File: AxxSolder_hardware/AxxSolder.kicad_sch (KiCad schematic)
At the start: 143 parts, among them IC1 TLV76733DRVR, IC2 OPA2387DSGT, IC3 LMR54406DBVR, IC4 STM32G431CBT6, IC5 TPD4E1U06DBVR, IC6 STUSB4500QTR, IC7 MAX16171ATA_VY+T, IC8 LTC4440AHMS8E, IC9 INA281A5QDBVRQ1, J1 USB4110-GF-A, J2 691243110009, J3 TSW-102-07-T-S, J4 61300611821, J5 TSW-102-07-T-S, J6 TSW-102-07-T-S, Q1 STL9P3LLH6, Q2 STL10N3LLH5, Q3 2N7002NXAKR, U2 PEC11J-9215F-S0015, U3 BSC014N04LS

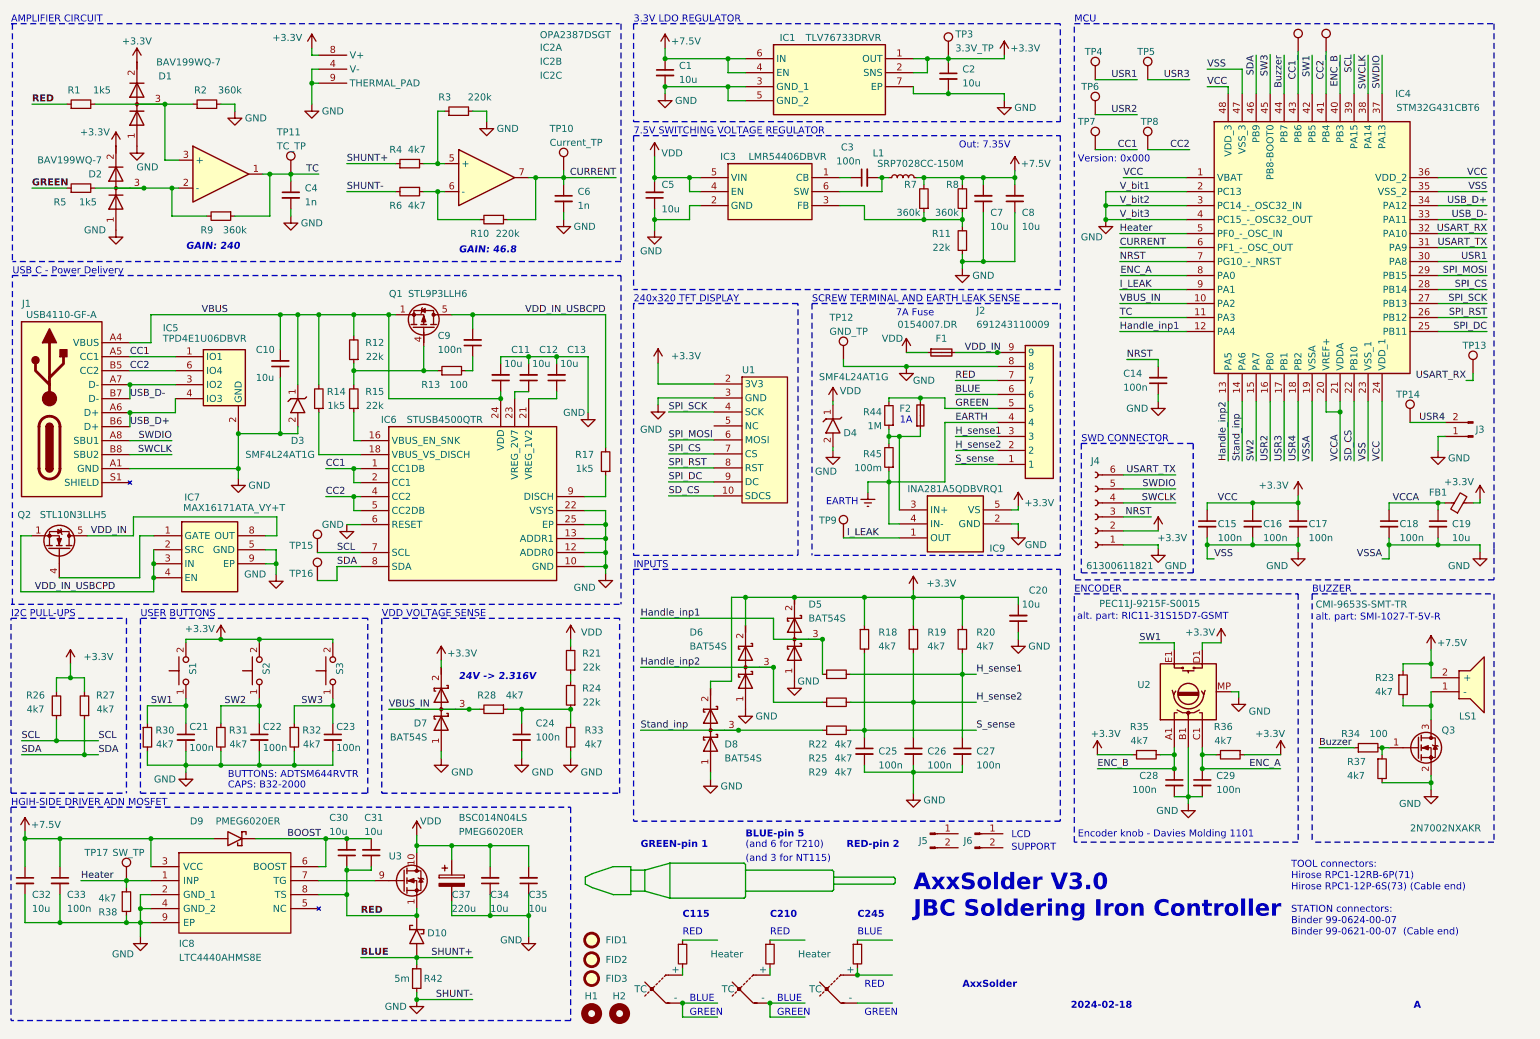
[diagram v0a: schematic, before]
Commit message: Create Lite version of board
Mark all USB-C components as DNP (except I2C pullups)
Swap LCD footprint from Adafruit 4311 to commodity GMT020-02 LCD
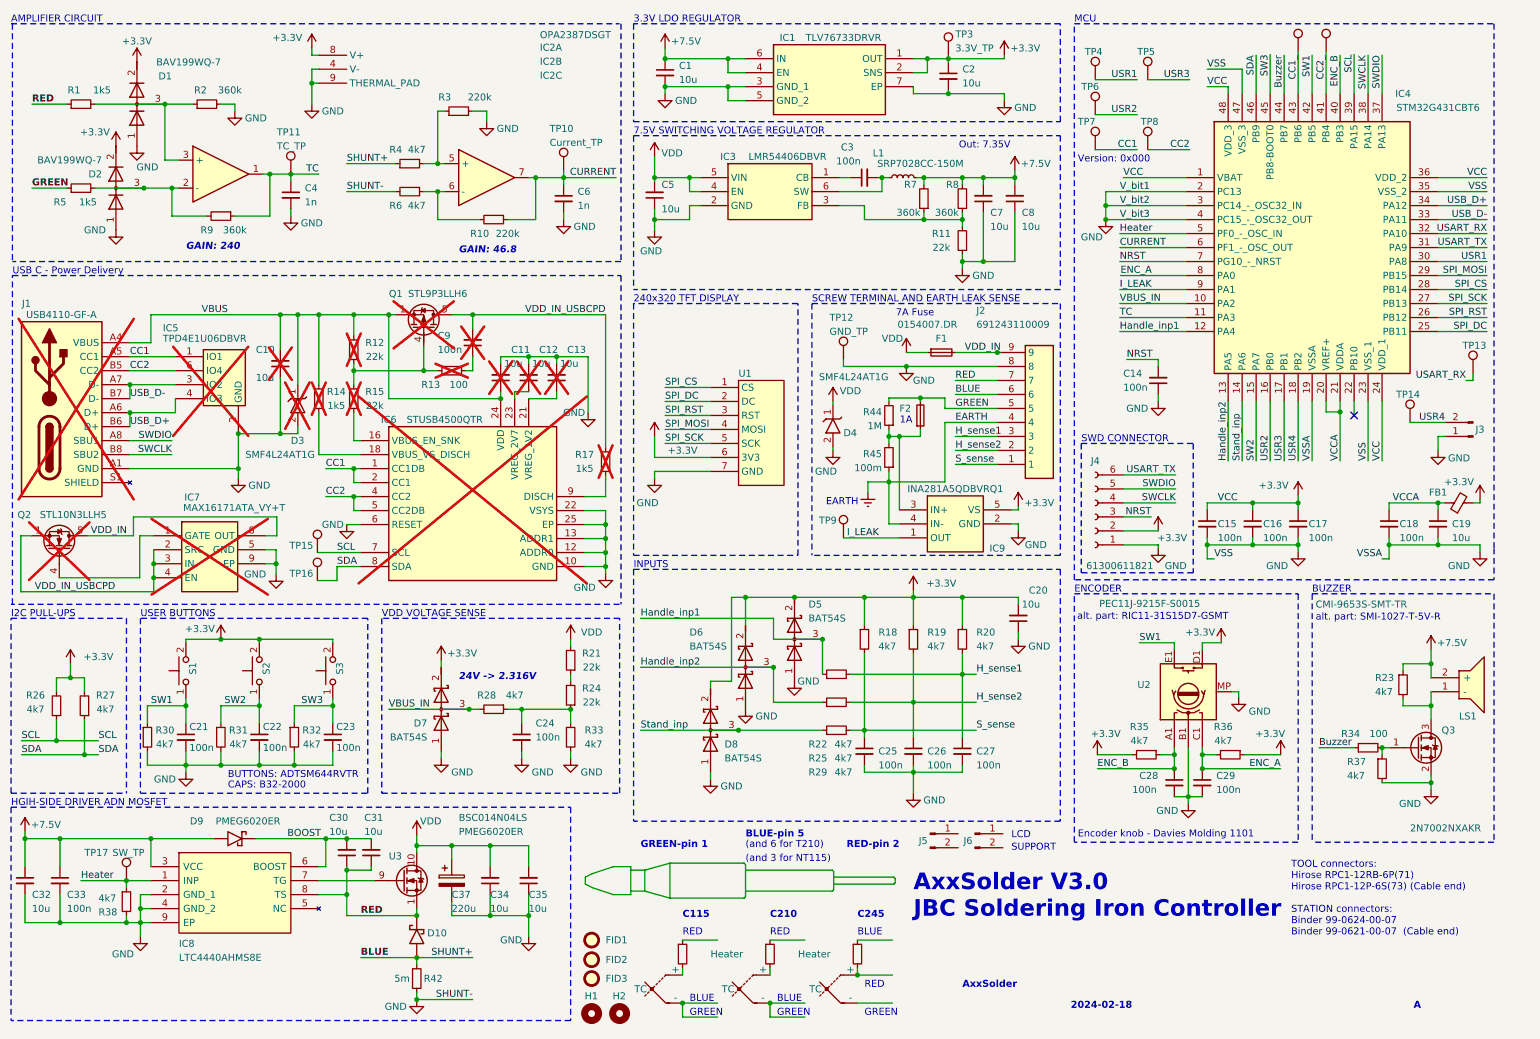
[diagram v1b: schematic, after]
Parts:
- C10, C11, C12, C13, C9, D3, IC6, IC7, Q1, Q2, R12, R13, R14, R15, R17: now not fitted; now left out of the parts list
- C37: footprint CAPAE830X1050N -> footprints:CAPAE830X1050N
- IC3: footprint SOT95P280X145-6N -> footprints:SOT95P280X145-6N
- IC5: footprint SOT95P280X145-6N -> footprints:SOT95P280X145-6N; now not fitted; now left out of the parts list
- J1: footprint USB4110GFA -> footprints:USB4110GFA; now not fitted; now left out of the parts list
- U1: footprint footprints:Adafruit_240x320_TFT -> Connector_PinHeader_2.54mm:PinHeader_1x07_P2.54mm_Vertical; Manufacturer_Name Adafruit -> (none); Manufacturer_Part_Number 4311 -> 2.0TFTSPI; Mouser Part Number 485-4311 -> (none); Mouser Price/Stock https://www.mouser.co.uk/ProductDetail/Adafruit/4311?qs=P1J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 -> (none)
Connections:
- net +3.3V: now also U1.6 (3V3); no longer U1.2 (3V3)
- net GND: now also U1.7 (GND); no longer U1.3 (GND)
- net SPI_CS: now also U1.1 (CS); no longer U1.7 (CS)
- net SPI_DC: now also U1.2 (DC); no longer U1.9 (DC)
- net SPI_MOSI: now also U1.4 (MOSI); no longer U1.6 (MOSI)
- net SPI_RST: now also U1.3 (RST); no longer U1.8 (RST)
- net SPI_SCK: now also U1.5 (SCK); no longer U1.4 (SCK)
- net SD_CS: no longer names the net of IC4.22 (PB10)
- net SD_CS: no longer U1.10 (SDCS)
- no-connect marks 0 -> 1

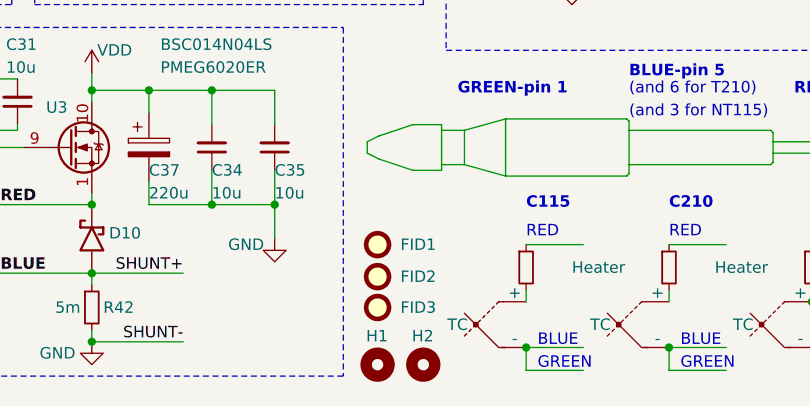
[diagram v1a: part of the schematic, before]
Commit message: Finish Lite modifications
Fix upper mounting holes (no longer align with display; now aligned to PCB)
Add GitHub link for licensing purposes (I think this is necesssary for GPL)
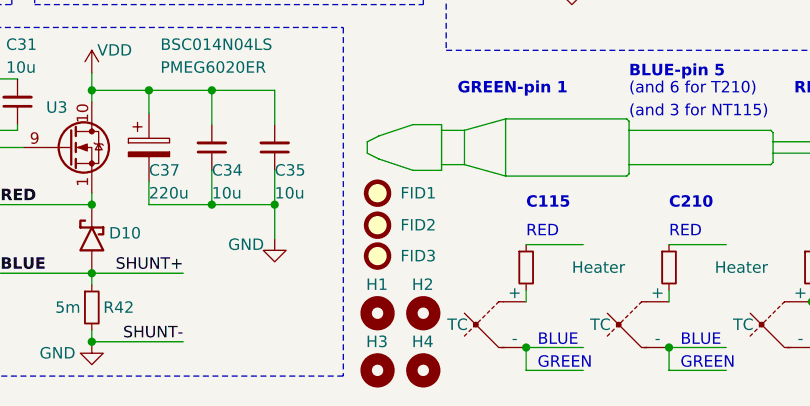
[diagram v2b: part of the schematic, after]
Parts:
- added H3, H4: MountingHole, MountingHole:MountingHole_2.5mm, symbol Mechanical:MountingHole
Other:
- moved on the sheet: FID1, FID2, FID3, H1, H2
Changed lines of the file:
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@@
     )
   )
+  (symbol (lib_id "Mechanical:MountingHole") (at 119.38 195.58 0) (unit 1)
+    (in_bom no) (on_board yes) (dnp no)
+    (property "Reference" "H3" (at 118.11 192.405 0)
+      (effects (font (size 1.27 1.27)) (justify left))
+    )
+    (property "Value" "MountingHole" (at 121.92 196.8499 0)
+      (effects (font (size 1.27 1.27)) (justify left) hide)
+    )
+    (property "Footprint" "MountingHole:MountingHole_2.5mm" (at 119.38 195.58 0)
+      (effects (font (size 1.27 1.27)) hide)
+    )
+    (property "Datasheet" "~" (at 119.38 195.58 0)
+      (effects (font (size 1.27 1.27)) hide)
+    )
+    (property "Assembly Comment" "N/A" (at 119.38 195.58 0)
+      (effects (font (size 1.27 1.27)) hide)
+    )
+    (property "Manufacturing comment" "Do Not Place" (at 119.38 195.58 0)
+      (effects (font (size 1.27 1.27)) hide)
+    )
+    (instances
+      (project "AxxSolder"
+        (path "/d71363c3-4d90-469c-a600-831e2a7cdaef"
+          (reference "H3") (unit 1)
+        )
+      )
+    )
+  )
   (symbol (lib_id "Connector:TestPoint") (at 252.73 20.32 0) (unit 1)
     (in_bom no) (on_board yes) (dnp no)
@@
     )
   )
-  (symbol (lib_id "Mechanical:MountingHole") (at 119.38 194.945 0) (unit 1)
+  (symbol (lib_id "Mechanical:MountingHole") (at 119.38 189.23 0) (unit 1)
     (in_bom no) (on_board yes) (dnp no)
-    (property "Reference" "H1" (at 118.11 191.77 0)
+    (property "Reference" "H1" (at 118.11 186.055 0)
       (effects (font (size 1.27 1.27)) (justify left))
     )
-    (property "Value" "MountingHole" (at 121.92 196.2149 0)
+    (property "Value" "MountingHole" (at 121.92 190.4999 0)
       (effects (font (size 1.27 1.27)) (justify left) hide)
     )
-    (property "Footprint" "MountingHole:MountingHole_2.5mm" (at 119.38 194.945 0)
+    (property "Footprint" "MountingHole:MountingHole_2.5mm" (at 119.38 189.23 0)
       (effects (font (size 1.27 1.27)) hide)
     )
-    (property "Datasheet" "~" (at 119.38 194.945 0)
+    (property "Datasheet" "~" (at 119.38 189.23 0)
       (effects (font (size 1.27 1.27)) hide)
     )
-    (property "Assembly Comment" "N/A" (at 119.38 194.945 0)
+    (property "Assembly Comment" "N/A" (at 119.38 189.23 0)
       (effects (font (size 1.27 1.27)) hide)
     )
-    (property "Manufacturing comment" "Do Not Place" (at 119.38 194.945 0)
+    (property "Manufacturing comment" "Do Not Place" (at 119.38 189.23 0)
       (effects (font (size 1.27 1.27)) hide)
     )
@@
     )
   )
-  (symbol (lib_id "Mechanical:Fiducial") (at 119.38 188.595 0) (unit 1)
+  (symbol (lib_id "Mechanical:Fiducial") (at 119.38 182.88 0) (unit 1)
     (in_bom no) (on_board yes) (dnp no)
-    (property "Reference" "FID3" (at 121.92 188.595 0)
+    (property "Reference" "FID3" (at 121.92 182.88 0)
       (effects (font (size 1.27 1.27)) (justify left))
     )
-    (property "Value" "Fiducial" (at 121.92 189.865 0)
+    (property "Value" "Fiducial" (at 121.92 184.15 0)
       (effects (font (size 1.27 1.27)) (justify left) hide)
     )
-    (property "Footprint" "Fiducial:Fiducial_0.75mm_Mask1.5mm" (at 119.38 188.595 0)
+    (property "Footprint" "Fiducial:Fiducial_0.75mm_Mask1.5mm" (at 119.38 182.88 0)
       (effects (font (size 1.27 1.27)) hide)
     )
-    (property "Datasheet" "~" (at 119.38 188.595 0)
+    (property "Datasheet" "~" (at 119.38 182.88 0)
       (effects (font (size 1.27 1.27)) hide)
     )
-    (property "Manufacturing comment" "Do Not Place" (at 119.38 188.595 0)
+    (property "Manufacturing comment" "Do Not Place" (at 119.38 182.88 0)
       (effects (font (size 1.27 1.27)) hide)
     )
@@
     )
   )
+  (symbol (lib_id "Mechanical:MountingHole") (at 124.46 195.58 0) (unit 1)
+    (in_bom no) (on_board yes) (dnp no)
+    (property "Reference" "H4" (at 123.19 192.405 0)
+      (effects (font (size 1.27 1.27)) (justify left))
+    )
+    (property "Value" "MountingHole" (at 127 196.8499 0)
+      (effects (font (size 1.27 1.27)) (justify left) hide)
+    )
+    (property "Footprint" "MountingHole:MountingHole_2.5mm" (at 124.46 195.58 0)
+      (effects (font (size 1.27 1.27)) hide)
+    )
+    (property "Datasheet" "~" (at 124.46 195.58 0)
+      (effects (font (size 1.27 1.27)) hide)
+    )
+    (property "Assembly Comment" "N/A" (at 124.46 195.58 0)
+      (effects (font (size 1.27 1.27)) hide)
+    )
+    (property "Manufacturing comment" "Do Not Place" (at 124.46 195.58 0)
+      (effects (font (size 1.27 1.27)) hide)
+    )
+    (instances
+      (project "AxxSolder"
+        (path "/d71363c3-4d90-469c-a600-831e2a7cdaef"
+          (reference "H4") (unit 1)
+        )
+      )
+    )
+  )
   (symbol (lib_id "power:GND") (at 247.65 111.125 0) (unit 1)
     (in_bom yes) (on_board yes) (dnp no)
@@
     )
   )
-  (symbol (lib_id "Mechanical:Fiducial") (at 119.38 185.166 0) (unit 1)
+  (symbol (lib_id "Mechanical:Fiducial") (at 119.38 179.451 0) (unit 1)
     (in_bom no) (on_board yes) (dnp no)
-    (property "Reference" "FID2" (at 121.92 185.166 0)
+    (property "Reference" "FID2" (at 121.92 179.451 0)
       (effects (font (size 1.27 1.27)) (justify left))
     )
-    (property "Value" "Fiducial" (at 121.92 186.436 0)
+    (property "Value" "Fiducial" (at 121.92 180.721 0)
       (effects (font (size 1.27 1.27)) (justify left) hide)
     )
-    (property "Footprint" "Fiducial:Fiducial_0.75mm_Mask1.5mm" (at 119.38 185.166 0)
+    (property "Footprint" "Fiducial:Fiducial_0.75mm_Mask1.5mm" (at 119.38 179.451 0)
       (effects (font (size 1.27 1.27)) hide)
     )
-    (property "Datasheet" "~" (at 119.38 185.166 0)
+    (property "Datasheet" "~" (at 119.38 179.451 0)
       (effects (font (size 1.27 1.27)) hide)
     )
-    (property "Manufacturing comment" "Do Not Place" (at 119.38 185.166 0)
+    (property "Manufacturing comment" "Do Not Place" (at 119.38 179.451 0)
       (effects (font (size 1.27 1.27)) hide)
     )
@@
     )
   )
-  (symbol (lib_id "Mechanical:Fiducial") (at 119.38 181.61 0) (unit 1)
+  (symbol (lib_id "Mechanical:Fiducial") (at 119.38 175.895 0) (unit 1)
     (in_bom no) (on_board yes) (dnp no)
-    (property "Reference" "FID1" (at 121.92 181.61 0)
+    (property "Reference" "FID1" (at 121.92 175.895 0)
       (effects (font (size 1.27 1.27)) (justify left))
     )
-    (property "Value" "Fiducial" (at 121.92 182.88 0)
+    (property "Value" "Fiducial" (at 121.92 177.165 0)
       (effects (font (size 1.27 1.27)) (justify left) hide)
     )
-    (property "Footprint" "Fiducial:Fiducial_0.75mm_Mask1.5mm" (at 119.38 181.61 0)
+    (property "Footprint" "Fiducial:Fiducial_0.75mm_Mask1.5mm" (at 119.38 175.895 0)
       (effects (font (size 1.27 1.27)) hide)
     )
-    (property "Datasheet" "~" (at 119.38 181.61 0)
+    (property "Datasheet" "~" (at 119.38 175.895 0)
       (effects (font (size 1.27 1.27)) hide)
     )
-    (property "Manufacturing comment" "Do Not Place" (at 119.38 181.61 0)
+    (property "Manufacturing comment" "Do Not Place" (at 119.38 175.895 0)
       (effects (font (size 1.27 1.27)) hide)
     )
@@
     )
   )
-  (symbol (lib_id "Mechanical:MountingHole") (at 124.46 194.945 0) (unit 1)
+  (symbol (lib_id "Mechanical:MountingHole") (at 124.46 189.23 0) (unit 1)
     (in_bom no) (on_board yes) (dnp no)
-    (property "Reference" "H2" (at 123.19 191.77 0)
+    (property "Reference" "H2" (at 123.19 186.055 0)
       (effects (font (size 1.27 1.27)) (justify left))
     )
-    (property "Value" "MountingHole" (at 127 196.2149 0)
+    (property "Value" "MountingHole" (at 127 190.4999 0)
       (effects (font (size 1.27 1.27)) (justify left) hide)
     )
-    (property "Footprint" "MountingHole:MountingHole_2.5mm" (at 124.46 194.945 0)
+    (property "Footprint" "MountingHole:MountingHole_2.5mm" (at 124.46 189.23 0)
       (effects (font (size 1.27 1.27)) hide)
     )
-    (property "Datasheet" "~" (at 124.46 194.945 0)
+    (property "Datasheet" "~" (at 124.46 189.23 0)
       (effects (font (size 1.27 1.27)) hide)
     )
-    (property "Assembly Comment" "N/A" (at 124.46 194.945 0)
+    (property "Assembly Comment" "N/A" (at 124.46 189.23 0)
       (effects (font (size 1.27 1.27)) hide)
     )
-    (property "Manufacturing comment" "Do Not Place" (at 124.46 194.945 0)
+    (property "Manufacturing comment" "Do Not Place" (at 124.46 189.23 0)
       (effects (font (size 1.27 1.27)) hide)
     )
